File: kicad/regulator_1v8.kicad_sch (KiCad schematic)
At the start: 3 parts, among them U1001 ADP122 1.8V

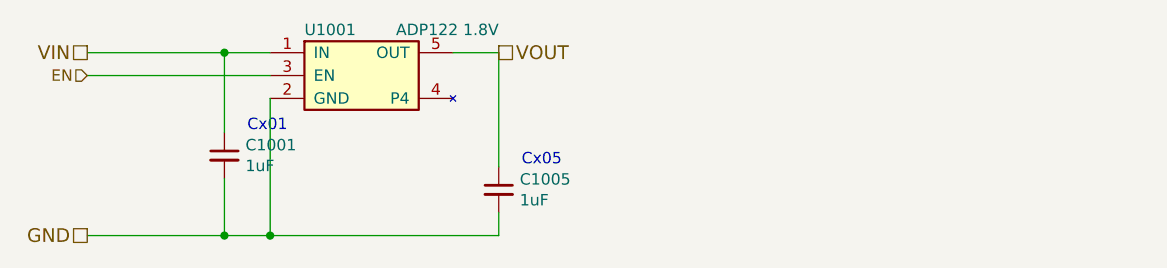
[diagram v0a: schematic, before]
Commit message: Broke down sensor block into a tree of sheets
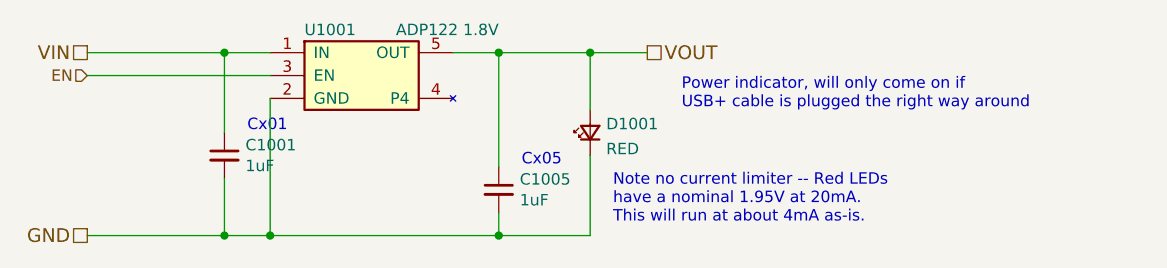
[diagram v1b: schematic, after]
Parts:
- added D1001: RED, LED_SMD:LED_0603_1608Metric, symbol Device:LED_Small
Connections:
- net GND: now also D1001.1 (K)
- net VOUT: now also D1001.2 (A)
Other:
- note added: "Note no current limiter -- Red LEDs have a nominal 1.95V at 20mA. This will run at about 4mA as-is."
- note added: "Power indicator, will only come on if USB+ cable is plugged the right way around"
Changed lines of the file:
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@@
 (kicad_sch (version 20211123) (generator eeschema)
   (paper "A4")
+  (junction (at 144.78 93.98) (diameter 0) (color 0 0 0 0)
+  )
+  (junction (at 154.94 93.98) (diameter 0) (color 0 0 0 0)
+  )
   (junction (at 114.3 93.98) (diameter 0) (color 0 0 0 0)
   )
@@
   )
   (junction (at 119.38 114.3) (diameter 0) (color 0 0 0 0)
+  )
+  (junction (at 144.78 114.3) (diameter 0) (color 0 0 0 0)
   )
   (wire (pts (xy 114.3 93.98) (xy 114.3 102.87))
@@
     (stroke (width 0) (type default) (color 0 0 0 0))
   )
-  (wire (pts (xy 144.78 106.68) (xy 144.78 93.98))
+  (wire (pts (xy 154.94 105.41) (xy 154.94 114.3))
     (stroke (width 0) (type default) (color 0 0 0 0))
   )
@@
     (stroke (width 0) (type default) (color 0 0 0 0))
   )
+  (wire (pts (xy 154.94 114.3) (xy 144.78 114.3))
+    (stroke (width 0) (type default) (color 0 0 0 0))
+  )
   (wire (pts (xy 99.06 93.98) (xy 114.3 93.98))
     (stroke (width 0) (type default) (color 0 0 0 0))
   )
-  (wire (pts (xy 144.78 93.98) (xy 139.7 93.98))
+  (wire (pts (xy 154.94 93.98) (xy 154.94 100.33))
+    (stroke (width 0) (type default) (color 0 0 0 0))
+  )
+  (wire (pts (xy 154.94 93.98) (xy 144.78 93.98))
+    (stroke (width 0) (type default) (color 0 0 0 0))
+  )
+  (wire (pts (xy 161.29 93.98) (xy 154.94 93.98))
     (stroke (width 0) (type default) (color 0 0 0 0))
   )
@@
     (stroke (width 0) (type default) (color 0 0 0 0))
   )
+  (wire (pts (xy 144.78 93.98) (xy 139.7 93.98))
+    (stroke (width 0) (type default) (color 0 0 0 0))
+  )
+  (wire (pts (xy 144.78 93.98) (xy 144.78 106.68))
+    (stroke (width 0) (type default) (color 0 0 0 0))
+  )
   (text "Cx01" (at 116.84 102.87 0)
+    (effects (font (size 1.27 1.27)) (justify left bottom))
+  )
+  (text "Power indicator, will only come on if\nUSB+ cable is plugged the right way around"
+    (at 165.1 100.33 0)
     (effects (font (size 1.27 1.27)) (justify left bottom))
   )
@@
     (effects (font (size 1.27 1.27)) (justify left bottom))
   )
-  (hierarchical_label "VOUT" (shape passive) (at 144.78 93.98 0)
+  (text "Note no current limiter -- Red LEDs\nhave a nominal 1.95V at 20mA. \nThis will run at about 4mA as-is."
+    (at 157.48 113.03 0)
+    (effects (font (size 1.27 1.27)) (justify left bottom))
+  )
+  (hierarchical_label "VOUT" (shape passive) (at 161.29 93.98 0)
     (effects (font (size 1.524 1.524)) (justify left))
   )
@@
       (effects (font (size 1.27 1.27)) hide)
     )
+    (pin "1")
+    (pin "2")
+  )
+  (symbol (lib_id "Device:LED_Small") (at 154.94 102.87 90)
+    (in_bom yes) (on_board yes) (fields_autoplaced)
+    (property "Reference" "D1001" (id 0) (at 156.718 101.898 90)
+      (effects (font (size 1.27 1.27)) (justify right))
+    )
+    (property "Value" "RED" (id 1) (at 156.718 104.6731 90)
+      (effects (font (size 1.27 1.27)) (justify right))
+    )
+    (property "Footprint" "LED_SMD:LED_0603_1608Metric" (id 2) (at 154.94 102.87 90)
+      (effects (font (size 1.27 1.27)) hide)
+    )
+    (property "Datasheet" "~" (id 3) (at 154.94 102.87 90)
+      (effects (font (size 1.27 1.27)) hide)
+    )

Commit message: Added Digikey references
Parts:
- C1001, C1005: Digikey (none) -> 399-C0402C105K9PAC7800CT-ND
- D1001: Digikey (none) -> 754-1123-1-ND; Purpose (none) -> Sensor block power indicator
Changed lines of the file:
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@@
       (effects (font (size 1.27 1.27)) hide)
     )
-    (property "Datasheet" "https://product.tdk.com/info/en/catalog/datasheets/mlcc_commercial_general_en.pdf" (id 3) (at 114.3 105.41 0)
+    (property "Datasheet" "~" (id 3) (at 114.3 105.41 0)
       (effects (font (size 1.27 1.27)) hide)
     )
-    (property "Digikey" "" (id 4) (at 114.3 105.41 0)
+    (property "Digikey" "399-C0402C105K9PAC7800CT-ND" (id 4) (at 114.3 105.41 0)
       (effects (font (size 1.27 1.27)) hide)
     )
@@
       (effects (font (size 1.27 1.27)) hide)
     )
-    (property "Datasheet" "https://product.tdk.com/info/en/catalog/datasheets/mlcc_commercial_general_en.pdf" (id 3) (at 144.78 109.22 0)
+    (property "Datasheet" "~" (id 3) (at 144.78 109.22 0)
       (effects (font (size 1.27 1.27)) hide)
     )
-    (property "Digikey" "" (id 4) (at 144.78 109.22 0)
+    (property "Digikey" "399-C0402C105K9PAC7800CT-ND" (id 4) (at 144.78 109.22 0)
       (effects (font (size 1.27 1.27)) hide)
     )
@@
       (effects (font (size 1.27 1.27)) hide)
     )
+    (property "Digikey" "754-1123-1-ND" (id 4) (at 154.94 102.87 0)
+      (effects (font (size 1.27 1.27)) hide)
+    )
+    (property "Purpose" "Sensor block power indicator" (id 5) (at 154.94 102.87 0)
+      (effects (font (size 1.27 1.27)) hide)
+    )

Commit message: One shining moment
Commit board while it still works
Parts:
- U3001: renamed from U1001; Purpose Regulator -> Regulator 3.3V->1.8V
- renumbered C1001 to C3001, C1005 to C3005, D1001 to D3001
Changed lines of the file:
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@@
   (symbol (lib_id "Device:C_Small") (at 114.3 105.41 0)
     (in_bom yes) (on_board yes)
-    (property "Reference" "C1001" (id 0) (at 116.6368 104.2416 0)
+    (property "Reference" "C3001" (id 0) (at 116.6368 104.2416 0)
       (effects (font (size 1.27 1.27)) (justify left))
     )
@@
   (symbol (lib_id "Device:C_Small") (at 144.78 109.22 0)
     (in_bom yes) (on_board yes)
-    (property "Reference" "C1005" (id 0) (at 147.1168 108.0516 0)
+    (property "Reference" "C3005" (id 0) (at 147.1168 108.0516 0)
       (effects (font (size 1.27 1.27)) (justify left))
     )
@@
   (symbol (lib_id "Device:LED_Small") (at 154.94 102.87 90)
     (in_bom yes) (on_board yes) (fields_autoplaced)
-    (property "Reference" "D1001" (id 0) (at 156.718 101.898 90)
+    (property "Reference" "D3001" (id 0) (at 156.718 101.898 90)
       (effects (font (size 1.27 1.27)) (justify right))
     )
@@
   (symbol (lib_id "KwanSystems:ADP122") (at 129.54 96.52 0)
     (in_bom yes) (on_board yes)
-    (property "Reference" "U1001" (id 0) (at 123.19 91.44 0)
+    (property "Reference" "U3001" (id 0) (at 123.19 91.44 0)
       (effects (font (size 1.27 1.27)) (justify left))
     )
@@
       (effects (font (size 1.27 1.27)) hide)
     )
-    (property "Purpose" "Regulator" (id 5) (at 129.54 96.52 0)
+    (property "Purpose" "Regulator 3.3V->1.8V" (id 5) (at 129.54 96.52 0)
       (effects (font (size 1.27 1.27)) hide)
     )

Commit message: Updated part number
Darn supply chain crisis :(
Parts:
- U3001: value ADP122 1.8V -> TCR2EF 1.8V; Digikey 505-ADP122AUJZ-3.3-R7CT-ND -> TCR2EF18LM(CTCT-ND
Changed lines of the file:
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@@
       (effects (font (size 1.27 1.27)) (justify left))
     )
-    (property "Value" "ADP122 1.8V" (id 1) (at 144.78 91.44 0)
+    (property "Value" "TCR2EF 1.8V" (id 1) (at 144.78 91.44 0)
       (effects (font (size 1.27 1.27)) (justify right))
     )
@@
       (effects (font (size 1.27 1.27)) hide)
     )
-    (property "Digikey" "505-ADP122AUJZ-3.3-R7CT-ND" (id 4) (at 129.54 96.52 0)
+    (property "Digikey" "TCR2EF18LM(CTCT-ND" (id 4) (at 129.54 96.52 0)
       (effects (font (size 1.27 1.27)) hide)
     )

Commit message: Updated purposes for regulators
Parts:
- C3001: Purpose Regulator Input -> 1.8V Regulator Input
- C3005: Purpose Shoulder Regulator output -> 1.8V Regulator output
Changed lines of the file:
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@@
       (effects (font (size 1.27 1.27)) hide)
     )
-    (property "Purpose" "Regulator Input" (id 5) (at 114.3 105.41 0)
+    (property "Purpose" "1.8V Regulator Input" (id 5) (at 114.3 105.41 0)
       (effects (font (size 1.27 1.27)) hide)
     )
@@
       (effects (font (size 1.27 1.27)) hide)
     )
-    (property "Purpose" "Shoulder Regulator output" (id 5) (at 144.78 109.22 0)
+    (property "Purpose" "1.8V Regulator output" (id 5) (at 144.78 109.22 0)
       (effects (font (size 1.27 1.27)) hide)
     )
